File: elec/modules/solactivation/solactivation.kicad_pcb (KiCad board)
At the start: 2 copper layers, 30.5 x 40.6 mm, 11 parts, among them J1 Conn_01x08, J2 Conn_01x08, J5 XT30, Q1 STP75NF75, Q2 IRLML6344TRPBF

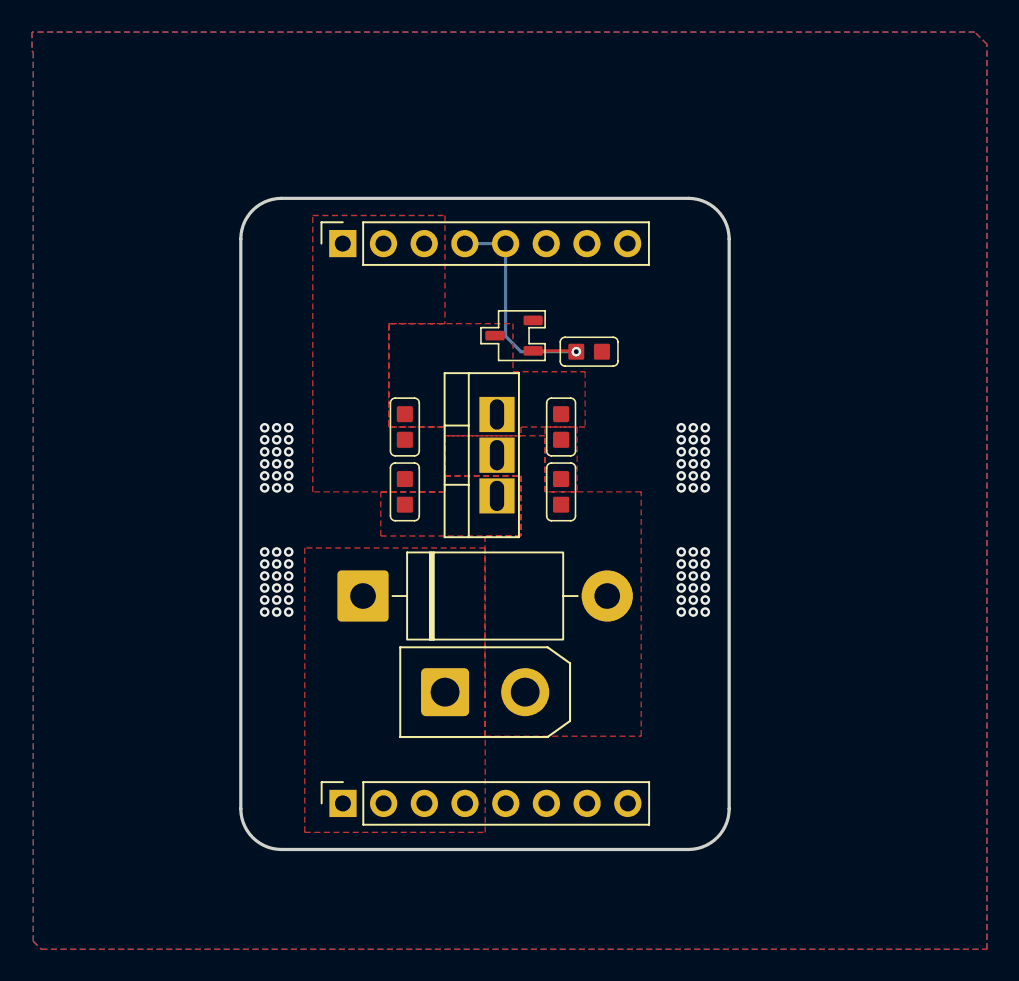
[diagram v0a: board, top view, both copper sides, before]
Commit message: added teardrops and sus via
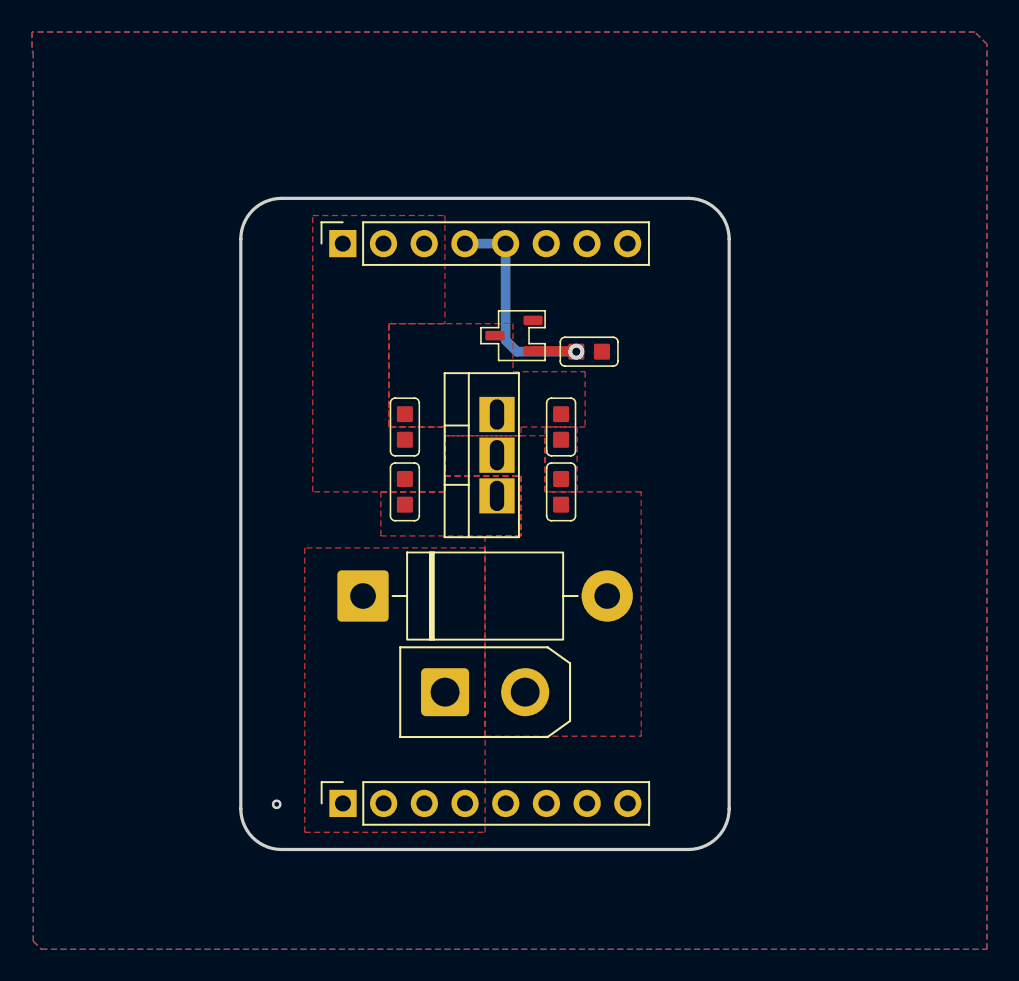
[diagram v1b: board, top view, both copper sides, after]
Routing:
- net GND: vias 72 -> 1

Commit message: added silkscreen
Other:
- board text added: "design of 2-Chairs. 2025 JLC Order No. JLCJLCJLCJLC"
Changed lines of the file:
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@@
 		(layer "Edge.Cuts")
+	)
+	(gr_text "design of 2-Chairs. 2025\nJLC Order No. JLCJLCJLCJLC"
+		(at 144.24 89.03 0)
+		(layer "B.SilkS")
+		(effects
+			(font
+				(size 1 1)
+				(thickness 0.2)
+			)
+			(justify mirror)
+		)
 	)
 	(segment
